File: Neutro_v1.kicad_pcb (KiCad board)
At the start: 4 copper layers, 101.6 x 63.5 mm, 61 parts, among them J1 SparkFun_Lipo_Converter, J2 Conn_Coaxial, U1 M20050-1, U2 RFM96W-433S2_1, U3 MS5803-01BA, U4 BNO080, U5 DS3231M_1

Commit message: neutro pcb v1 final design 1.21.22
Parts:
- C5: value locked -> 10u
- moved TP16 0.50 mm to (197.0, 96.5)
- moved R10 0.30 mm to (186.4, 103.3)
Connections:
- net Net-(C1-Pad2) renamed /gps_pwr
- net Net-(C5-Pad2) renamed /t_pwr
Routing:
- net /gps_pwr: track 18.3 -> 0.00 mm, vias 6 -> 8
- net /t_pwr: track 5.86 -> 0.00 mm, vias 2 -> 8
- net +3.3V: track 11.5 -> 6.22 mm, vias 7 -> 11
- net GND: track 7.55 -> 7.83 mm, vias 18 -> 35
- added copper zone on F.Cu, net +3.3V
- added copper zone on F.Cu, net /gps_pwr
- added copper zone on In1.Cu, net /gps_pwr
- added copper zone on F.Cu, net /t_pwr
- added copper zone on In1.Cu, net /t_pwr
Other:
- board text added: "x"
- board text added: "y"
- board text added: "z"

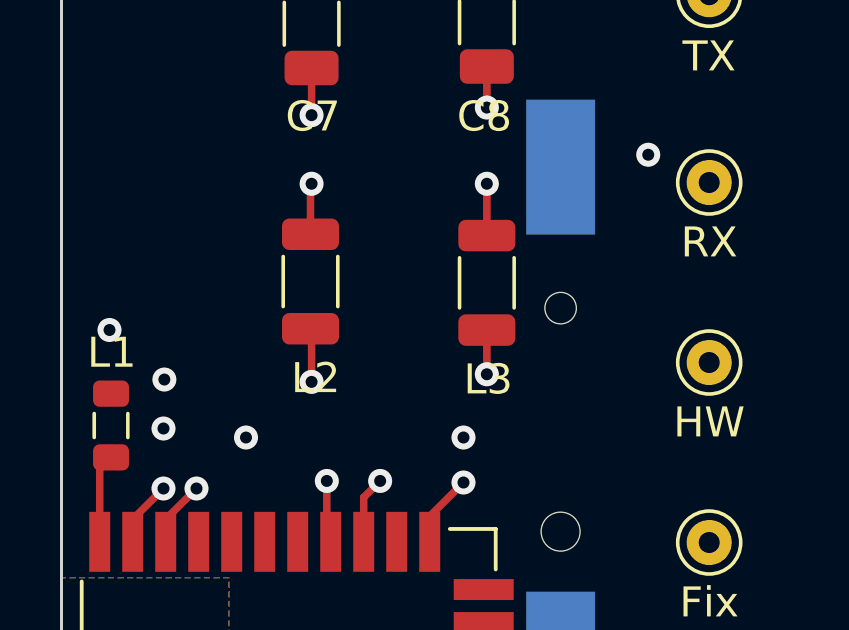
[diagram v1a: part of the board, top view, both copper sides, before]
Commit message: neutro v1 1.21.23 final pcb (change L2, L3 size)
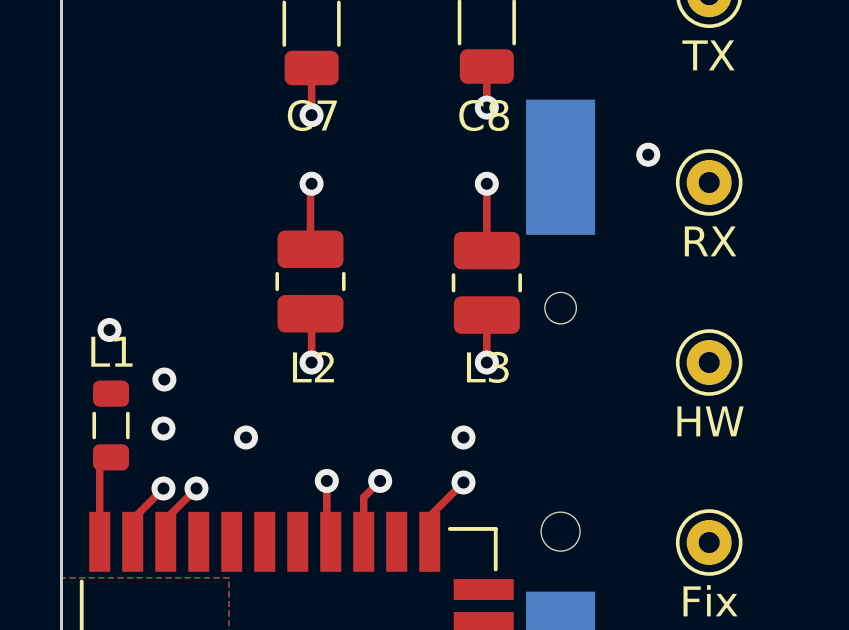
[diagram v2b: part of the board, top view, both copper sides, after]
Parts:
- L2, L3: footprint Inductor_SMD:L_1206_3216Metric -> Inductor_SMD:L_1008_2520Metric
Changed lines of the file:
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@@
       (net 4 "GND") (pinfunction "1") (pintype "passive"))
   )
-  (footprint "Inductor_SMD:L_1206_3216Metric" (layer "F.Cu")
+  (footprint "Inductor_SMD:L_1008_2520Metric" (layer "F.Cu")
     (at 115.777998 88.3435 90)
-    (descr "Inductor SMD 1206 (3216 Metric), square (rectangular) end terminal, IPC_7351 nominal, (Body size source: IPC-SM-782 page 80, https://www.pcb-3d.com/wordpress/wp-content/uploads/ipc-sm-782a_amendment_1_and_2.pdf), generated with kicad-footprint-generator")
+    (descr "Inductor SMD 1008 (2520 Metric), square (rectangular) end terminal, IPC_7351 nominal, (Body size source: https://ecsxtal.com/store/pdf/ECS-MPI2520-SMD-POWER-INDUCTOR.pdf), generated with kicad-footprint-generator")
     (tags "inductor")
     (property "Sheetfile" "Neutro_v1.kicad_sch")
     (property "Sheetname" "")
     (attr smd)
-    (fp_text reference "L3" (at -3.2235 0.046002 180) (layer "F.SilkS")
-      (effects (font (size 1 1) (thickness 0.15)))
-    )
-    (fp_text value "47n" (at 2.9995 0.046002 180) (layer "F.Fab")
-      (effects (font (size 1 1) (thickness 0.15)))
-    )
-    (fp_text user "${REFERENCE}" (at 0 0 180) (layer "F.Fab")
-      (effects (font (size 0.8 0.8) (thickness 0.12)))
-    )
-    (fp_line (start -0.835242 0.91) (end 0.835242 0.91) (layer "F.SilkS") (width 0.12))
-    (fp_line (start -0.835242 -0.91) (end 0.835242 -0.91) (layer "F.SilkS") (width 0.12))
-    (fp_line (start 2.35 1.2) (end -2.35 1.2) (layer "F.CrtYd") (width 0.05))
-    (fp_line (start 2.35 -1.2) (end 2.35 1.2) (layer "F.CrtYd") (width 0.05))
-    (fp_line (start -2.35 -1.2) (end 2.35 -1.2) (layer "F.CrtYd") (width 0.05))
-    (fp_line (start -2.35 1.2) (end -2.35 -1.2) (layer "F.CrtYd") (width 0.05))
-    (fp_line (start -1.6 -0.8) (end 1.6 -0.8) (layer "F.Fab") (width 0.1))
-    (fp_line (start 1.6 0.8) (end -1.6 0.8) (layer "F.Fab") (width 0.1))
-    (fp_line (start -1.6 0.8) (end -1.6 -0.8) (layer "F.Fab") (width 0.1))
-    (fp_line (start 1.6 -0.8) (end 1.6 0.8) (layer "F.Fab") (width 0.1))
-    (pad "1" smd roundrect (at -1.575 0 90) (size 1.05 1.9) (layers "F.Cu" "F.Paste" "F.Mask") (roundrect_rratio 0.2380952381)
+    (fp_text reference "L3" (at -2.8565 0.022002 180) (layer "F.SilkS")
+      (effects (font (size 1 1) (thickness 0.15)))
+    )
+    (fp_text value "47n" (at -0.0565 2.822002 180) (layer "F.Fab")
+      (effects (font (size 1 1) (thickness 0.15)))
+    )
+    (fp_text user "${REFERENCE}" (at 0 0 90) (layer "F.Fab")
+      (effects (font (size 0.62 0.62) (thickness 0.09)))
+    )
+    (fp_line (start -0.261252 1.11) (end 0.261252 1.11) (layer "F.SilkS") (width 0.12))
+    (fp_line (start -0.261252 -1.11) (end 0.261252 -1.11) (layer "F.SilkS") (width 0.12))
+    (fp_line (start 1.95 1.35) (end -1.95 1.35) (layer "F.CrtYd") (width 0.05))
+    (fp_line (start -1.95 1.35) (end -1.95 -1.35) (layer "F.CrtYd") (width 0.05))
+    (fp_line (start -1.95 -1.35) (end 1.95 -1.35) (layer "F.CrtYd") (width 0.05))
+    (fp_line (start 1.95 -1.35) (end 1.95 1.35) (layer "F.CrtYd") (width 0.05))
+    (fp_line (start 1.25 1) (end -1.25 1) (layer "F.Fab") (width 0.1))
+    (fp_line (start 1.25 -1) (end 1.25 1) (layer "F.Fab") (width 0.1))
+    (fp_line (start -1.25 1) (end -1.25 -1) (layer "F.Fab") (width 0.1))
+    (fp_line (start -1.25 -1) (end 1.25 -1) (layer "F.Fab") (width 0.1))
+    (pad "1" smd roundrect (at -1.075 0 90) (size 1.25 2.2) (layers "F.Cu" "F.Paste" "F.Mask") (roundrect_rratio 0.2)
       (net 28 "Net-(L3-Pad1)") (pintype "passive"))
-    (pad "2" smd roundrect (at 1.575 0 90) (size 1.05 1.9) (layers "F.Cu" "F.Paste" "F.Mask") (roundrect_rratio 0.2380952381)
+    (pad "2" smd roundrect (at 1.075 0 90) (size 1.25 2.2) (layers "F.Cu" "F.Paste" "F.Mask") (roundrect_rratio 0.2)
       (net 7 "TX") (pintype "passive"))
-    (model "${KICAD6_3DMODEL_DIR}/Inductor_SMD.3dshapes/L_1206_3216Metric.wrl"
+    (model "${KICAD6_3DMODEL_DIR}/Inductor_SMD.3dshapes/L_1008_2520Metric.wrl"
       (offset (xyz 0 0 0))
       (scale (xyz 1 1 1))
@@
     )
   )
-  (footprint "Inductor_SMD:L_1206_3216Metric" (layer "F.Cu")
+  (footprint "Inductor_SMD:L_1008_2520Metric" (layer "F.Cu")
     (at 109.9 88.3 90)
-    (descr "Inductor SMD 1206 (3216 Metric), square (rectangular) end terminal, IPC_7351 nominal, (Body size source: IPC-SM-782 page 80, https://www.pcb-3d.com/wordpress/wp-content/uploads/ipc-sm-782a_amendment_1_and_2.pdf), generated with kicad-footprint-generator")
+    (descr "Inductor SMD 1008 (2520 Metric), square (rectangular) end terminal, IPC_7351 nominal, (Body size source: https://ecsxtal.com/store/pdf/ECS-MPI2520-SMD-POWER-INDUCTOR.pdf), generated with kicad-footprint-generator")
     (tags "inductor")
     (property "Sheetfile" "Neutro_v1.kicad_sch")
     (property "Sheetname" "")
     (attr smd)
-    (fp_text reference "L2" (at -3.2235 0.173002) (layer "F.SilkS")
-      (effects (font (size 1 1) (thickness 0.15)))
-    )
-    (fp_text value "47n" (at 2.9995 0.046002) (layer "F.Fab")
-      (effects (font (size 1 1) (thickness 0.15)))
-    )
-    (fp_text user "${REFERENCE}" (at 0 0) (layer "F.Fab")
-      (effects (font (size 0.8 0.8) (thickness 0.12)))
-    )
-    (fp_line (start -0.835242 -0.91) (end 0.835242 -0.91) (layer "F.SilkS") (width 0.12))
-    (fp_line (start -0.835242 0.91) (end 0.835242 0.91) (layer "F.SilkS") (width 0.12))
-    (fp_line (start -2.35 -1.2) (end 2.35 -1.2) (layer "F.CrtYd") (width 0.05))
-    (fp_line (start -2.35 1.2) (end -2.35 -1.2) (layer "F.CrtYd") (width 0.05))
-    (fp_line (start 2.35 1.2) (end -2.35 1.2) (layer "F.CrtYd") (width 0.05))
-    (fp_line (start 2.35 -1.2) (end 2.35 1.2) (layer "F.CrtYd") (width 0.05))
-    (fp_line (start 1.6 -0.8) (end 1.6 0.8) (layer "F.Fab") (width 0.1))
-    (fp_line (start 1.6 0.8) (end -1.6 0.8) (layer "F.Fab") (width 0.1))
-    (fp_line (start -1.6 0.8) (end -1.6 -0.8) (layer "F.Fab") (width 0.1))
-    (fp_line (start -1.6 -0.8) (end 1.6 -0.8) (layer "F.Fab") (width 0.1))
-    (pad "1" smd roundrect (at -1.575 0 90) (size 1.05 1.9) (layers "F.Cu" "F.Paste" "F.Mask") (roundrect_rratio 0.2380952381)
+    (fp_text reference "L2" (at -2.9 0.1 180) (layer "F.SilkS")
+      (effects (font (size 1 1) (thickness 0.15)))
+    )
+    (fp_text value "47n" (at 0 2.7 180) (layer "F.Fab")
+      (effects (font (size 1 1) (thickness 0.15)))
+    )
+    (fp_text user "${REFERENCE}" (at 0 0 90) (layer "F.Fab")
+      (effects (font (size 0.62 0.62) (thickness 0.09)))
+    )
+    (fp_line (start -0.261252 -1.11) (end 0.261252 -1.11) (layer "F.SilkS") (width 0.12))
+    (fp_line (start -0.261252 1.11) (end 0.261252 1.11) (layer "F.SilkS") (width 0.12))
+    (fp_line (start -1.95 1.35) (end -1.95 -1.35) (layer "F.CrtYd") (width 0.05))
+    (fp_line (start 1.95 1.35) (end -1.95 1.35) (layer "F.CrtYd") (width 0.05))
+    (fp_line (start -1.95 -1.35) (end 1.95 -1.35) (layer "F.CrtYd") (width 0.05))
+    (fp_line (start 1.95 -1.35) (end 1.95 1.35) (layer "F.CrtYd") (width 0.05))
+    (fp_line (start 1.25 1) (end -1.25 1) (layer "F.Fab") (width 0.1))
+    (fp_line (start -1.25 1) (end -1.25 -1) (layer "F.Fab") (width 0.1))
+    (fp_line (start 1.25 -1) (end 1.25 1) (layer "F.Fab") (width 0.1))
+    (fp_line (start -1.25 -1) (end 1.25 -1) (layer "F.Fab") (width 0.1))
+    (pad "1" smd roundrect (at -1.075 0 90) (size 1.25 2.2) (layers "F.Cu" "F.Paste" "F.Mask") (roundrect_rratio 0.2)
       (net 27 "Net-(L2-Pad1)") (pintype "passive"))
-    (pad "2" smd roundrect (at 1.575 0 90) (size 1.05 1.9) (layers "F.Cu" "F.Paste" "F.Mask") (roundrect_rratio 0.2380952381)
+    (pad "2" smd roundrect (at 1.075 0 90) (size 1.25 2.2) (layers "F.Cu" "F.Paste" "F.Mask") (roundrect_rratio 0.2)
       (net 6 "RX") (pintype "passive"))
-    (model "${KICAD6_3DMODEL_DIR}/Inductor_SMD.3dshapes/L_1206_3216Metric.wrl"
+    (model "${KICAD6_3DMODEL_DIR}/Inductor_SMD.3dshapes/L_1008_2520Metric.wrl"
       (offset (xyz 0 0 0))
       (scale (xyz 1 1 1))
@@
   (segment (start 109.935998 89.910998) (end 109.9 89.875) (width 0.25) (layer "F.Cu") (net 27))
   (segment (start 110.443998 94.9475) (end 110.443998 96.8475) (width 0.25) (layer "F.Cu") (net 27))
-  (segment (start 109.935998 91.6455) (end 109.935998 89.910998) (width 0.25) (layer "F.Cu") (net 27))
+  (segment (start 109.935998 91) (end 109.935998 89.910998) (width 0.25) (layer "F.Cu") (net 27))
   (via (at 110.443998 94.9475) (size 0.8) (drill 0.4) (layers "F.Cu" "B.Cu") (net 27))
-  (via (at 109.935998 91.6455) (size 0.8) (drill 0.4) (layers "F.Cu" "B.Cu") (net 27))
-  (segment (start 110.443998 92.1535) (end 109.935998 91.6455) (width 0.25) (layer "In1.Cu") (net 27))
-  (segment (start 110.443998 94.9475) (end 110.443998 92.1535) (width 0.25) (layer "In1.Cu") (net 27))
+  (via (at 109.935998 91) (size 0.8) (drill 0.4) (layers "F.Cu" "B.Cu") (net 27))
+  (segment (start 109.935998 91) (end 110.443998 91.508) (width 0.25) (layer "In1.Cu") (net 27))
+  (segment (start 110.443998 91.508) (end 110.443998 94.9475) (width 0.25) (layer "In1.Cu") (net 27))
+  (segment (start 115.777998 89.9185) (end 115.777998 91) (width 0.25) (layer "F.Cu") (net 28))
   (segment (start 112.221998 94.9475) (end 111.673998 95.4955) (width 0.25) (layer "F.Cu") (net 28))
   (segment (start 111.673998 95.4955) (end 111.673998 96.9775) (width 0.25) (layer "F.Cu") (net 28))
-  (segment (start 115.777998 89.9185) (end 115.777998 91.3915) (width 0.25) (layer "F.Cu") (net 28))
-  (via (at 115.777998 91.3915) (size 0.8) (drill 0.4) (layers "F.Cu" "B.Cu") (net 28))
+  (via (at 115.777998 91) (size 0.8) (drill 0.4) (layers "F.Cu" "B.Cu") (net 28))
   (via (at 112.221998 94.9475) (size 0.8) (drill 0.4) (layers "F.Cu" "B.Cu") (net 28))
+  (segment (start 115.777998 91.3915) (end 115.777998 91) (width 0.25) (layer "In1.Cu") (net 28))
   (segment (start 112.221998 94.9475) (end 115.777998 91.3915) (width 0.25) (layer "In1.Cu") (net 28))
   (segment (start 196.125 102.35) (end 196.137 102.362) (width 0.25) (layer "F.Cu") (net 29))
